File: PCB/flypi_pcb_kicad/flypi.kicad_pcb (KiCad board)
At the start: 2 copper layers, 76.1 x 85 mm, 45 parts, among them CON1 BARREL_JACK, J12 USB_A, P1 PeltS1S2, P10 RGB RG-B, P3 Fan+-, P4 Therm +s-, P5 HP1+-, P6 HP2+-, P7 servo +s-, P8 Ring +-s, P9 I2C +-scsd, Q1 1A_NPN_EBC, Q2 1A-NPN-EBC, Q3 1A_NPN_EBC, Q4 1A_NPN_EBC, U1 LM2596, U2 LM2596, U4 L298N, U5 arduino_mini

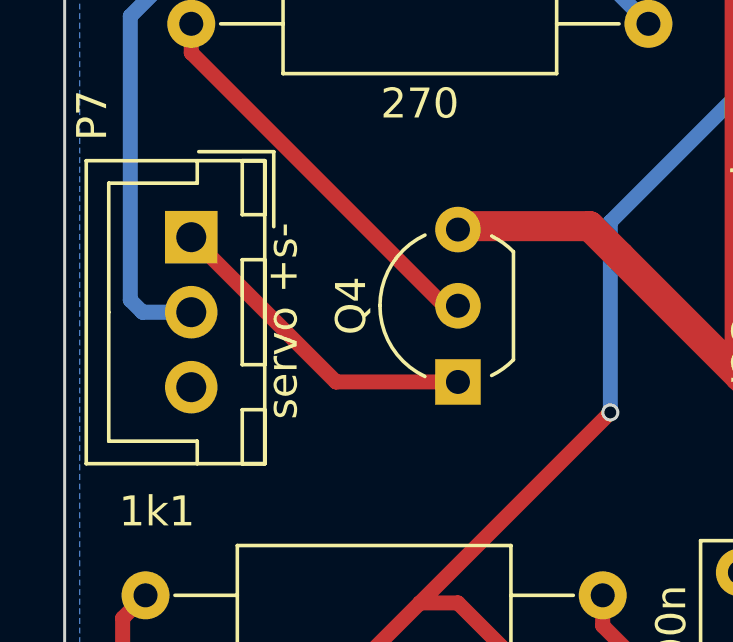
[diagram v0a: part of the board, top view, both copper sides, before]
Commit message: fix  misslabeling on board
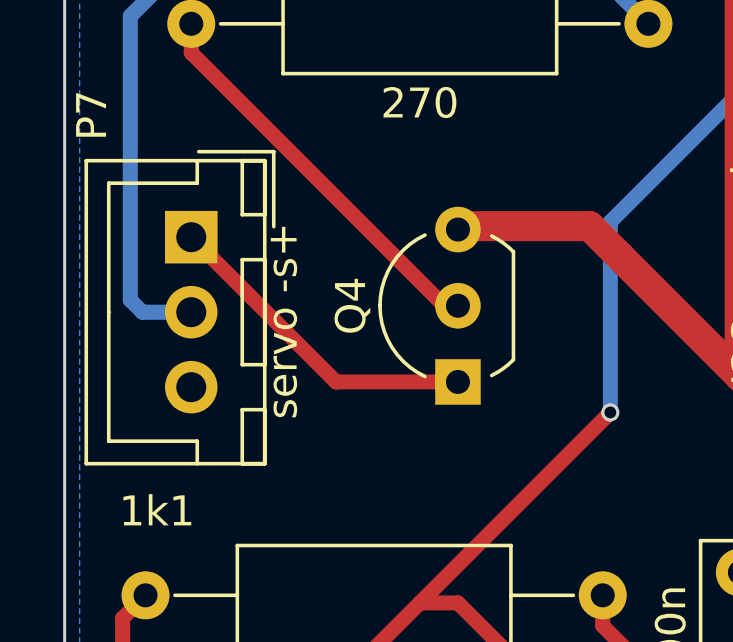
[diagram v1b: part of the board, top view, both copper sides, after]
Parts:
- P7: value servo +s- -> servo -s+
